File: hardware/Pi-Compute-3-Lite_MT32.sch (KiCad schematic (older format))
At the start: 0 parts

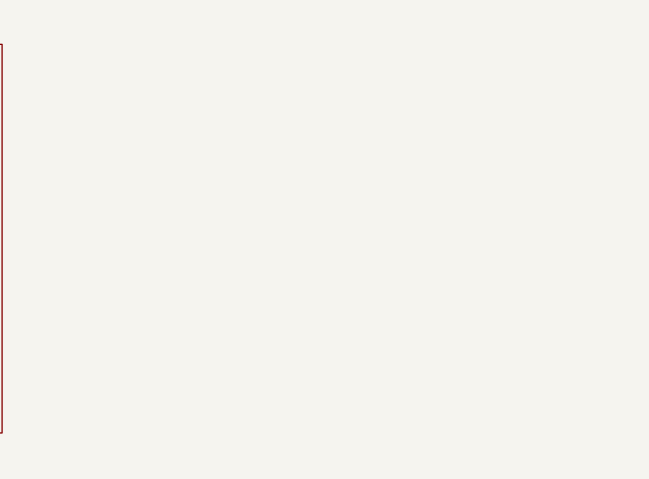
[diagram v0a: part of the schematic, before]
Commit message: Cleaning up the power section
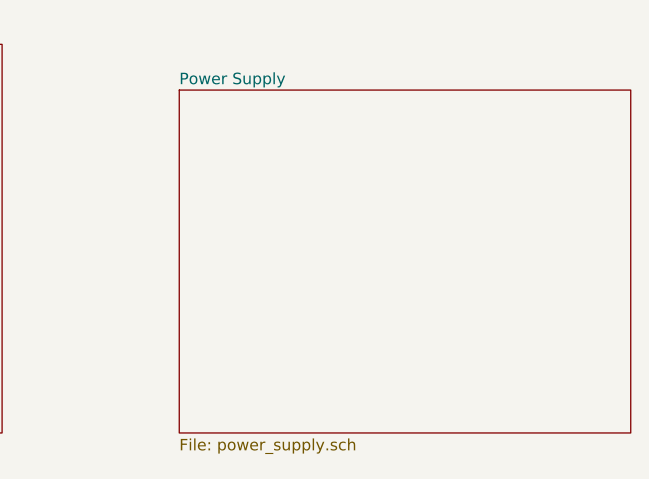
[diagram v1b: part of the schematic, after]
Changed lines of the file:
@@
 $Descr A 11000 8500
 encoding utf-8
-Sheet 1 3
+Sheet 1 4
 Title ""
 Date ""
@@
 F1 "audio-dac.sch" 50
 $EndSheet
+$Sheet
+S 6175 1375 1975 1500
+U 614BED8F
+F0 "Power Supply" 50
+F1 "power_supply.sch" 50
+$EndSheet
 $EndSCHEMATC
